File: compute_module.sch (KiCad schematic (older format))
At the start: 24 parts, among them Q1 2N7002P.215

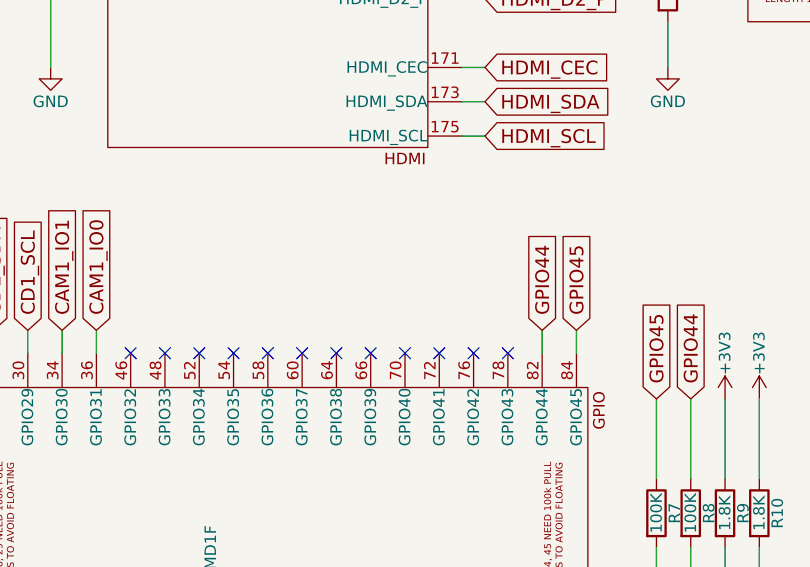
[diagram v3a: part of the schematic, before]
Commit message: Added audio jack
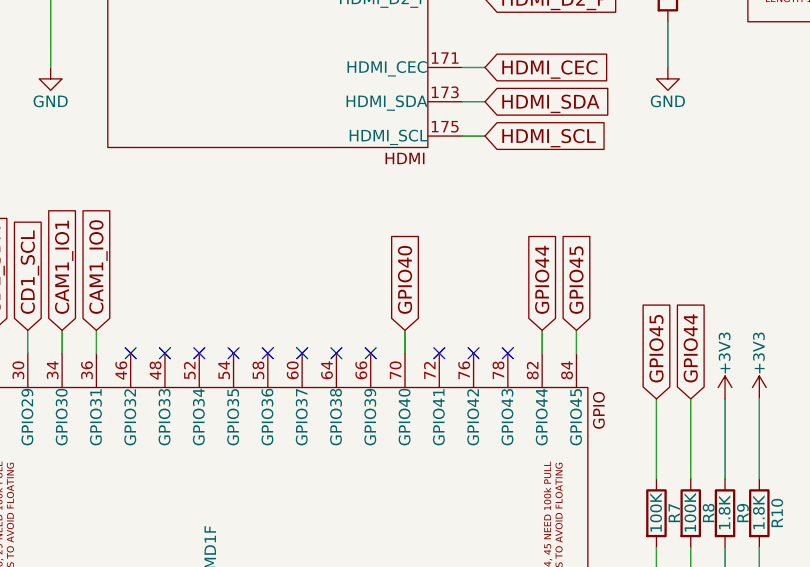
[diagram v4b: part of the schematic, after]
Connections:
- net GPIO40: now reaches MD1.70 (GPIO40)
- no-connect marks 42 -> 41
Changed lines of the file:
@@
 LIBS:REG1117
 LIBS:dk_USB-DVI-HDMI-Connectors
+LIBS:jack_trs_5pins
 LIBS:compute_module-cache
 EELAYER 25 0
@@
 HDMI_HPD_N_1V8
 $Comp
-L GND #PWR6
+L GND #PWR01
 U 1 1 5C0F0CA0
 P 3250 7600
-F 0 "#PWR6" H 3250 7350 50  0001 C CNN
+F 0 "#PWR01" H 3250 7350 50  0001 C CNN
 F 1 "GND" H 3250 7450 50  0000 C CNN
 F 2 "" H 3250 7600 50  0000 C CNN
@@
 $EndComp
 $Comp
-L GND #PWR5
+L GND #PWR02
 U 1 1 5C0F250C
 P 1350 7600
-F 0 "#PWR5" H 1350 7350 50  0001 C CNN
+F 0 "#PWR02" H 1350 7350 50  0001 C CNN
 F 1 "GND" H 1350 7450 50  0000 C CNN
 F 2 "" H 1350 7600 50  0000 C CNN
@@
 $EndComp
 $Comp
-L +1V8 #PWR4
+L +1V8 #PWR03
 U 1 1 5C0F4C79
 P 1250 850
-F 0 "#PWR4" H 1250 700 50  0001 C CNN
+F 0 "#PWR03" H 1250 700 50  0001 C CNN
 F 1 "+1V8" V 1250 1050 50  0000 C CNN
 F 2 "" H 1250 850 50  0000 C CNN
@@
 $EndComp
 $Comp
-L +3V3 #PWR3
+L +3V3 #PWR04
 U 1 1 5C0F4D26
 P 1150 850
-F 0 "#PWR3" H 1150 700 50  0001 C CNN
+F 0 "#PWR04" H 1150 700 50  0001 C CNN
 F 1 "+3V3" V 1150 1050 50  0000 C CNN
 F 2 "" H 1150 850 50  0000 C CNN
@@
 $EndComp
 $Comp
-L +5V #PWR2
+L +5V #PWR05
 U 1 1 5C0F51BB
 P 1050 850
-F 0 "#PWR2" H 1050 700 50  0001 C CNN
+F 0 "#PWR05" H 1050 700 50  0001 C CNN
 F 1 "+5V" V 1050 1050 50  0000 C CNN
 F 2 "" H 1050 850 50  0000 C CNN
@@
 $EndSheet
 $Comp
-L +1V8 #PWR7
+L +1V8 #PWR06
 U 1 1 5C11BA0E
 P 3550 6650
-F 0 "#PWR7" H 3550 6500 50  0001 C CNN
+F 0 "#PWR06" H 3550 6500 50  0001 C CNN
 F 1 "+1V8" V 3550 6850 50  0000 C CNN
 F 2 "" H 3550 6650 50  0000 C CNN
@@
 $EndComp
 $Comp
-L GND #PWR8
+L GND #PWR07
 U 1 1 5C11BBDE
 P 3550 7600
-F 0 "#PWR8" H 3550 7350 50  0001 C CNN
+F 0 "#PWR07" H 3550 7350 50  0001 C CNN
 F 1 "GND" H 3550 7450 50  0000 C CNN
 F 2 "" H 3550 7600 50  0000 C CNN
@@
 $EndComp
 $Comp
-L +1V8 #PWR10
+L +1V8 #PWR08
 U 1 1 5C11BD14
 P 3750 6650
-F 0 "#PWR10" H 3750 6500 50  0001 C CNN
+F 0 "#PWR08" H 3750 6500 50  0001 C CNN
 F 1 "+1V8" V 3750 6850 50  0000 C CNN
 F 2 "" H 3750 6650 50  0000 C CNN
@@
 $EndComp
 $Comp
-L GND #PWR11
+L GND #PWR09
 U 1 1 5C11BD1B
 P 3750 7600
-F 0 "#PWR11" H 3750 7350 50  0001 C CNN
+F 0 "#PWR09" H 3750 7350 50  0001 C CNN
 F 1 "GND" H 3750 7450 50  0000 C CNN
 F 2 "" H 3750 7600 50  0000 C CNN
@@
 $EndComp
 $Comp
-L GND #PWR19
+L GND #PWR010
 U 1 1 5C11BDDB
 P 4350 7600
-F 0 "#PWR19" H 4350 7350 50  0001 C CNN
+F 0 "#PWR010" H 4350 7350 50  0001 C CNN
 F 1 "GND" H 4350 7450 50  0000 C CNN
 F 2 "" H 4350 7600 50  0000 C CNN
@@
 $EndComp
 $Comp
-L GND #PWR23
+L GND #PWR011
 U 1 1 5C11BDEF
 P 4550 7600
-F 0 "#PWR23" H 4550 7350 50  0001 C CNN
+F 0 "#PWR011" H 4550 7350 50  0001 C CNN
 F 1 "GND" H 4550 7450 50  0000 C CNN
 F 2 "" H 4550 7600 50  0000 C CNN
@@
 $EndComp
 $Comp
-L +3V3 #PWR18
+L +3V3 #PWR012
 U 1 1 5C11BEF4
 P 4350 6650
-F 0 "#PWR18" H 4350 6500 50  0001 C CNN
+F 0 "#PWR012" H 4350 6500 50  0001 C CNN
 F 1 "+3V3" V 4350 6850 50  0000 C CNN
 F 2 "" H 4350 6650 50  0000 C CNN
@@
 $EndComp
 $Comp
-L +3V3 #PWR22
+L +3V3 #PWR013
 U 1 1 5C11BF29
 P 4550 6650
-F 0 "#PWR22" H 4550 6500 50  0001 C CNN
+F 0 "#PWR013" H 4550 6500 50  0001 C CNN
 F 1 "+3V3" V 4550 6850 50  0000 C CNN
 F 2 "" H 4550 6650 50  0000 C CNN
@@
 $EndComp
 $Comp
-L GND #PWR25
+L GND #PWR014
 U 1 1 5C11C06B
 P 4750 7600
-F 0 "#PWR25" H 4750 7350 50  0001 C CNN
+F 0 "#PWR014" H 4750 7350 50  0001 C CNN
 F 1 "GND" H 4750 7450 50  0000 C CNN
 F 2 "" H 4750 7600 50  0000 C CNN
@@
 $EndComp
 $Comp
-L GND #PWR27
+L GND #PWR015
 U 1 1 5C11C079
 P 4950 7600
-F 0 "#PWR27" H 4950 7350 50  0001 C CNN
+F 0 "#PWR015" H 4950 7350 50  0001 C CNN
 F 1 "GND" H 4950 7450 50  0000 C CNN
 F 2 "" H 4950 7600 50  0000 C CNN
@@
 $EndComp
 $Comp
-L +5V #PWR24
+L +5V #PWR016
 U 1 1 5C11C1E6
 P 4750 6650
-F 0 "#PWR24" H 4750 6500 50  0001 C CNN
+F 0 "#PWR016" H 4750 6500 50  0001 C CNN
 F 1 "+5V" V 4750 6850 50  0000 C CNN
 F 2 "" H 4750 6650 50  0000 C CNN
@@
 $EndComp
 $Comp
-L +5V #PWR26
+L +5V #PWR017
 U 1 1 5C11C2A1
 P 4950 6650
-F 0 "#PWR26" H 4950 6500 50  0001 C CNN
+F 0 "#PWR017" H 4950 6500 50  0001 C CNN
 F 1 "+5V" V 4950 6850 50  0000 C CNN
 F 2 "" H 4950 6650 50  0000 C CNN
@@
 $EndComp
 $Comp
-L GND #PWR17
+L GND #PWR018
 U 1 1 5C11C3B5
 P 4150 7600
-F 0 "#PWR17" H 4150 7350 50  0001 C CNN
+F 0 "#PWR018" H 4150 7350 50  0001 C CNN
 F 1 "GND" H 4150 7450 50  0000 C CNN
 F 2 "" H 4150 7600 50  0000 C CNN
@@
 $EndComp
 $Comp
-L GND #PWR13
+L GND #PWR019
 U 1 1 5C11C683
 P 3950 7600
-F 0 "#PWR13" H 3950 7350 50  0001 C CNN
+F 0 "#PWR019" H 3950 7350 50  0001 C CNN
 F 1 "GND" H 3950 7450 50  0000 C CNN
 F 2 "" H 3950 7600 50  0000 C CNN
@@
 $EndSheet
 $Comp
-L GND #PWR37
+L GND #PWR020
 U 1 1 5C0F98E0
 P 7250 2400
-F 0 "#PWR37" H 7250 2150 50  0001 C CNN
+F 0 "#PWR020" H 7250 2150 50  0001 C CNN
 F 1 "GND" H 7250 2250 50  0000 C CNN
 F 2 "" H 7250 2400 50  0000 C CNN
@@
 $EndComp
 $Comp
-L +3V3 #PWR14
+L +3V3 #PWR021
 U 1 1 5C12FB4C
 P 4100 850
-F 0 "#PWR14" H 4100 700 50  0001 C CNN
+F 0 "#PWR021" H 4100 700 50  0001 C CNN
 F 1 "+3V3" V 4100 1050 50  0000 C CNN
 F 2 "" H 4100 850 50  0000 C CNN
@@
 $EndComp
 $Comp
-L GND #PWR15
+L GND #PWR022
 U 1 1 5C131038
 P 4100 2400
-F 0 "#PWR15" H 4100 2150 50  0001 C CNN
+F 0 "#PWR022" H 4100 2150 50  0001 C CNN
 F 1 "GND" H 4100 2250 50  0000 C CNN
 F 2 "" H 4100 2400 50  0000 C CNN
@@
 NoConn ~ 6400 3650
 NoConn ~ 6250 3650
-NoConn ~ 6100 3650
 NoConn ~ 5950 3650
 NoConn ~ 5800 3650
@@
 $EndComp
 $Comp
-L +1V8 #PWR9
+L +1V8 #PWR023
 U 1 1 5C141105
 P 3650 850
-F 0 "#PWR9" H 3650 700 50  0001 C CNN
+F 0 "#PWR023" H 3650 700 50  0001 C CNN
 F 1 "+1V8" V 3650 1050 50  0000 C CNN
 F 2 "" H 3650 850 50  0000 C CNN
@@
 $EndComp
 $Comp
-L +3V3 #PWR1
+L +3V3 #PWR024
 U 1 1 5C195AE7
 P 950 850
-F 0 "#PWR1" H 950 700 50  0001 C CNN
+F 0 "#PWR024" H 950 700 50  0001 C CNN
 F 1 "+3V3" V 950 1050 50  0000 C CNN
 F 2 "" H 950 850 50  0000 C CNN
@@
 $EndComp
 $Comp
-L +3V3 #PWR16
+L +3V3 #PWR025
 U 1 1 5C195EED
 P 4150 6650
-F 0 "#PWR16" H 4150 6500 50  0001 C CNN
+F 0 "#PWR025" H 4150 6500 50  0001 C CNN
 F 1 "+3V3" V 4150 6850 50  0000 C CNN
 F 2 "" H 4150 6650 50  0000 C CNN
@@
 $EndComp
 $Comp
-L +3V3 #PWR12
+L +3V3 #PWR026
 U 1 1 5C195F34
 P 3950 6650
-F 0 "#PWR12" H 3950 6500 50  0001 C CNN
+F 0 "#PWR026" H 3950 6500 50  0001 C CNN
 F 1 "+3V3" V 3950 6850 50  0000 C CNN
 F 2 "" H 3950 6650 50  0000 C CNN
@@
 $EndComp
 $Comp
-L GND #PWR31
+L GND #PWR027
 U 1 1 5C197E23
 P 5350 7600
-F 0 "#PWR31" H 5350 7350 50  0001 C CNN
+F 0 "#PWR027" H 5350 7350 50  0001 C CNN
 F 1 "GND" H 5350 7450 50  0000 C CNN
 F 2 "" H 5350 7600 50  0000 C CNN
@@
 $EndComp
 $Comp
-L GND #PWR29
+L GND #PWR028
 U 1 1 5C197E2F
 P 5150 7600
-F 0 "#PWR29" H 5150 7350 50  0001 C CNN
+F 0 "#PWR028" H 5150 7350 50  0001 C CNN
 F 1 "GND" H 5150 7450 50  0000 C CNN
 F 2 "" H 5150 7600 50  0000 C CNN
@@
 $EndComp
 $Comp
-L +3V3 #PWR30
+L +3V3 #PWR029
 U 1 1 5C197E3F
 P 5350 6650
-F 0 "#PWR30" H 5350 6500 50  0001 C CNN
+F 0 "#PWR029" H 5350 6500 50  0001 C CNN
 F 1 "+3V3" V 5350 6850 50  0000 C CNN
 F 2 "" H 5350 6650 50  0000 C CNN
@@
 $EndComp
 $Comp
-L +3V3 #PWR28
+L +3V3 #PWR030
 U 1 1 5C197E45
 P 5150 6650
-F 0 "#PWR28" H 5150 6500 50  0001 C CNN
+F 0 "#PWR030" H 5150 6500 50  0001 C CNN
 F 1 "+3V3" V 5150 6850 50  0000 C CNN
 F 2 "" H 5150 6650 50  0000 C CNN
@@
 $EndComp
 $Comp
-L GND #PWR35
+L GND #PWR031
 U 1 1 5C1991D7
 P 5750 7600
-F 0 "#PWR35" H 5750 7350 50  0001 C CNN
+F 0 "#PWR031" H 5750 7350 50  0001 C CNN
 F 1 "GND" H 5750 7450 50  0000 C CNN
 F 2 "" H 5750 7600 50  0000 C CNN
@@
 $EndComp
 $Comp
-L GND #PWR33
+L GND #PWR032
 U 1 1 5C1991E3
 P 5550 7600
-F 0 "#PWR33" H 5550 7350 50  0001 C CNN
+F 0 "#PWR032" H 5550 7350 50  0001 C CNN
 F 1 "GND" H 5550 7450 50  0000 C CNN
 F 2 "" H 5550 7600 50  0000 C CNN
@@
 $EndComp
 $Comp
-L +3V3 #PWR34
+L +3V3 #PWR033
 U 1 1 5C1991F3
 P 5750 6650
-F 0 "#PWR34" H 5750 6500 50  0001 C CNN
+F 0 "#PWR033" H 5750 6500 50  0001 C CNN
 F 1 "+3V3" V 5750 6850 50  0000 C CNN
 F 2 "" H 5750 6650 50  0000 C CNN
@@
 $EndComp
 $Comp
-L +3V3 #PWR32
+L +3V3 #PWR034
 U 1 1 5C1991F9
 P 5550 6650
-F 0 "#PWR32" H 5550 6500 50  0001 C CNN
+F 0 "#PWR034" H 5550 6500 50  0001 C CNN
 F 1 "+3V3" V 5550 6850 50  0000 C CNN
 F 2 "" H 5550 6650 50  0000 C CNN
@@
 $EndComp
 $Comp
-L +3V3 #PWR39
+L +3V3 #PWR035
 U 1 1 5C19C417
 P 7500 3850
-F 0 "#PWR39" H 7500 3700 50  0001 C CNN
+F 0 "#PWR035" H 7500 3700 50  0001 C CNN
 F 1 "+3V3" V 7500 4050 50  0000 C CNN
 F 2 "" H 7500 3850 50  0000 C CNN
@@
 $EndComp
 $Comp
-L +3V3 #PWR40
+L +3V3 #PWR036
 U 1 1 5C19C476
 P 7650 3850
-F 0 "#PWR40" H 7650 3700 50  0001 C CNN
+F 0 "#PWR036" H 7650 3700 50  0001 C CNN
 F 1 "+3V3" V 7650 4050 50  0000 C CNN
 F 2 "" H 7650 3850 50  0000 C CNN
@@
 	4550 1250 4550 1350
 $Comp
-L +3V3 #PWR20
+L +3V3 #PWR037
 U 1 1 5C1D8C6B
 P 4550 850
-F 0 "#PWR20" H 4550 700 50  0001 C CNN
+F 0 "#PWR037" H 4550 700 50  0001 C CNN
 F 1 "+3V3" V 4550 1050 50  0000 C CNN
 F 2 "" H 4550 850 50  0000 C CNN
@@
 	4550 850  4550 950
 $Comp
-L GND #PWR21
+L GND #PWR038
 U 1 1 5C1D8DF6
 P 4550 2400
-F 0 "#PWR21" H 4550 2150 50  0001 C CNN
+F 0 "#PWR038" H 4550 2150 50  0001 C CNN
 F 1 "GND" H 4550 2250 50  0000 C CNN
 F 2 "" H 4550 2400 50  0000 C CNN
@@
 	4550 1650 4550 2400
 $Comp
-L GND #PWR?
+L GND #PWR039
 U 1 1 5C1D87F3
 P 7200 4850
-F 0 "#PWR?" H 7200 4600 50  0001 C CNN
+F 0 "#PWR039" H 7200 4600 50  0001 C CNN
 F 1 "GND" H 7200 4700 50  0000 C CNN
 F 2 "" H 7200 4850 50  0000 C CNN
@@
 $EndComp
 $Comp
-L GND #PWR?
+L GND #PWR040
 U 1 1 5C1D8894
 P 7350 4850
-F 0 "#PWR?" H 7350 4600 50  0001 C CNN
+F 0 "#PWR040" H 7350 4600 50  0001 C CNN
 F 1 "GND" H 7350 4700 50  0000 C CNN
 F 2 "" H 7350 4850 50  0000 C CNN
@@
 	1    0    0    -1
 $EndComp
+Text GLabel 6100 3550 1    60   Input ~ 0
+GPIO40
+Wire Wire Line
+	6100 3550 6100 3650
 $EndSCHEMATC

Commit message: Cleaned up libs
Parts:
- MD1: footprint footprints:Conn_TE-DDR2-SODIMM-0.6-200P-doublesided -> Conn_TE-DDR2-SODIMM:Conn_TE-DDR2-SODIMM-0.6-200P-doublesided
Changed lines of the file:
@@
 F 0 "MD1" H 1700 750 50  0000 C CNN
 F 1 "Board_RPi_CM3_200pConnector_multipart" H 2300 7600 50  0000 C CNN
-F 2 "footprints:Conn_TE-DDR2-SODIMM-0.6-200P-doublesided" H 8275 1300 10  0001 C CNN
+F 2 "Conn_TE-DDR2-SODIMM:Conn_TE-DDR2-SODIMM-0.6-200P-doublesided" H 8275 1300 10  0001 C CNN
 F 3 "_" H 8275 1300 10  0001 C CNN
 F 4 "_" H 8275 1300 10  0001 C CNN "Manf#"
@@
 F 0 "MD1" H 10300 3350 50  0000 C CNN
 F 1 "Board_RPi_CM3_200pConnector_multipart" H 10300 3650 50  0000 C CNN
-F 2 "footprints:Conn_TE-DDR2-SODIMM-0.6-200P-doublesided" H 16275 500 10  0001 C CNN
+F 2 "Conn_TE-DDR2-SODIMM:Conn_TE-DDR2-SODIMM-0.6-200P-doublesided" H 16275 500 10  0001 C CNN
 F 3 "_" H 16275 500 10  0001 C CNN
 F 4 "_" H 16275 500 10  0001 C CNN "Manf#"
@@
 F 0 "MD1" H 10350 5150 50  0000 C CNN
 F 1 "Board_RPi_CM3_200pConnector_multipart" H 10350 6500 50  0000 C CNN
-F 2 "footprints:Conn_TE-DDR2-SODIMM-0.6-200P-doublesided" H 16325 2300 10  0001 C CNN
+F 2 "Conn_TE-DDR2-SODIMM:Conn_TE-DDR2-SODIMM-0.6-200P-doublesided" H 16325 2300 10  0001 C CNN
 F 3 "_" H 16325 2300 10  0001 C CNN
 F 4 "_" H 16325 2300 10  0001 C CNN "Manf#"
@@
 F 0 "MD1" H 5500 1800 50  0000 C CNN
 F 1 "Board_RPi_CM3_200pConnector_multipart" H 5550 3000 50  0000 C CNN
-F 2 "footprints:Conn_TE-DDR2-SODIMM-0.6-200P-doublesided" H 11475 -1050 10  0001 C CNN
+F 2 "Conn_TE-DDR2-SODIMM:Conn_TE-DDR2-SODIMM-0.6-200P-doublesided" H 11475 -1050 10  0001 C CNN
 F 3 "_" H 11475 -1050 10  0001 C CNN
 F 4 "_" H 11475 -1050 10  0001 C CNN "Manf#"
@@
 F 0 "MD1" H 8300 1550 50  0000 C CNN
 F 1 "Board_RPi_CM3_200pConnector_multipart" H 8300 2400 50  0000 C CNN
-F 2 "footprints:Conn_TE-DDR2-SODIMM-0.6-200P-doublesided" H 14275 -1350 10  0001 C CNN
+F 2 "Conn_TE-DDR2-SODIMM:Conn_TE-DDR2-SODIMM-0.6-200P-doublesided" H 14275 -1350 10  0001 C CNN
 F 3 "_" H 14275 -1350 10  0001 C CNN
 F 4 "_" H 14275 -1350 10  0001 C CNN "Manf#"
@@
 F 0 "MD1" H 10300 1800 50  0000 C CNN
 F 1 "Board_RPi_CM3_200pConnector_multipart" H 10350 3000 50  0000 C CNN
-F 2 "footprints:Conn_TE-DDR2-SODIMM-0.6-200P-doublesided" H 16275 -1050 10  0001 C CNN
+F 2 "Conn_TE-DDR2-SODIMM:Conn_TE-DDR2-SODIMM-0.6-200P-doublesided" H 16275 -1050 10  0001 C CNN
 F 3 "_" H 16275 -1050 10  0001 C CNN
 F 4 "_" H 16275 -1050 10  0001 C CNN "Manf#"
@@
 F 0 "MD1" H 5200 4450 50  0000 C CNN
 F 1 "Board_RPi_CM3_200pConnector_multipart" H 5250 6300 50  0000 C CNN
-F 2 "footprints:Conn_TE-DDR2-SODIMM-0.6-200P-doublesided" H 11175 1650 10  0001 C CNN
+F 2 "Conn_TE-DDR2-SODIMM:Conn_TE-DDR2-SODIMM-0.6-200P-doublesided" H 11175 1650 10  0001 C CNN
 F 3 "_" H 11175 1650 10  0001 C CNN
 F 4 "_" H 11175 1650 10  0001 C CNN "Manf#"

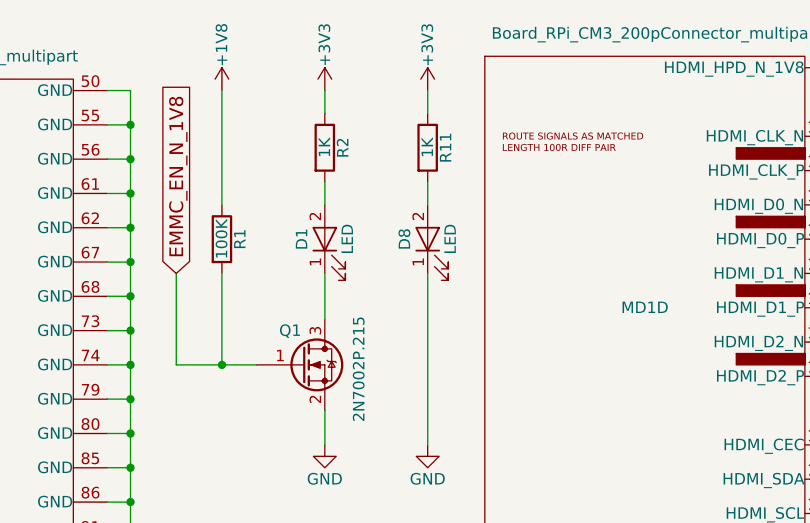
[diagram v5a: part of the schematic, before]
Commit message: Replaced 1uF input cap with 100nF
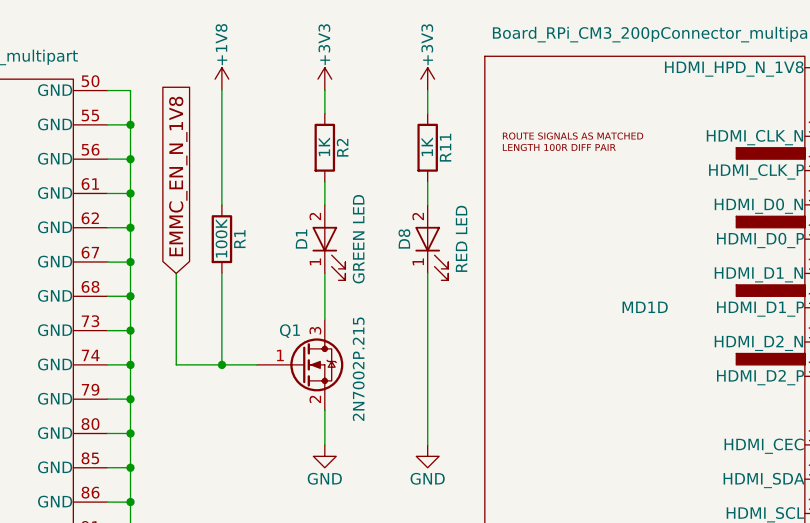
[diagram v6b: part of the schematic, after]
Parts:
- D1: value LED -> GREEN LED
- D8: value LED -> RED LED
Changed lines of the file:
@@
 P 4100 1500
 F 0 "D1" H 4100 1600 50  0000 C CNN
-F 1 "LED" H 4100 1400 50  0000 C CNN
+F 1 "GREEN LED" H 4100 1350 50  0000 C CNN
 F 2 "LEDs:LED_0805" H 4100 1500 50  0001 C CNN
 F 3 "" H 4100 1500 50  0000 C CNN
@@
 P 4550 1500
 F 0 "D8" H 4550 1600 50  0000 C CNN
-F 1 "LED" H 4550 1400 50  0000 C CNN
+F 1 "RED LED" H 4550 1350 50  0000 C CNN
 F 2 "LEDs:LED_0805" H 4550 1500 50  0001 C CNN
 F 3 "" H 4550 1500 50  0000 C CNN
